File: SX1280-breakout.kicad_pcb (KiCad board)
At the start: 2 copper layers, 16 x 16 mm, 32 parts, among them J1 Conn_01x01, J10 Conn_01x01, J11 Conn_01x01, J12 Conn_01x01, J13 Conn_01x01, J14 Conn_01x01, J15 Conn_01x01, J16 Conn_01x01, J2 Conn_01x01, J3 Conn_01x01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

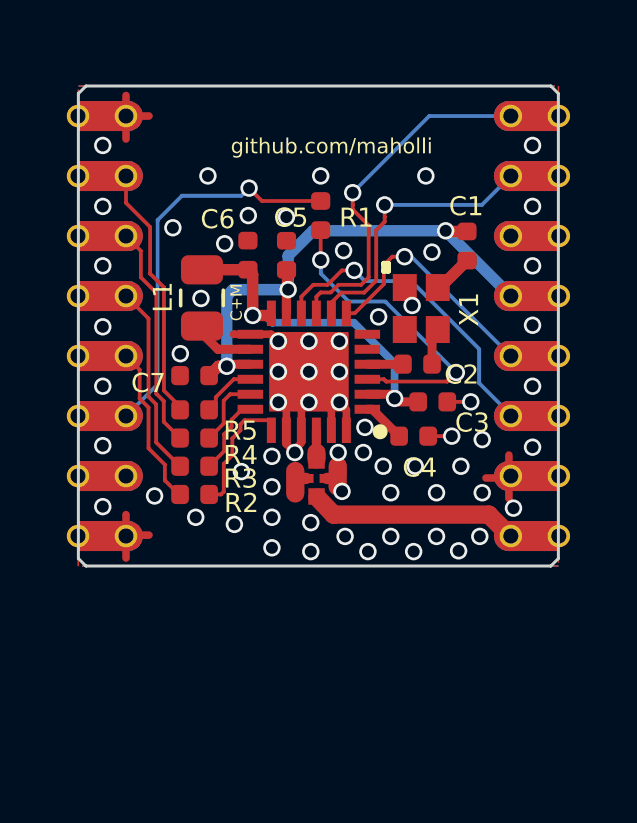
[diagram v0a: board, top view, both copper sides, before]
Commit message: fixing TCXO cap
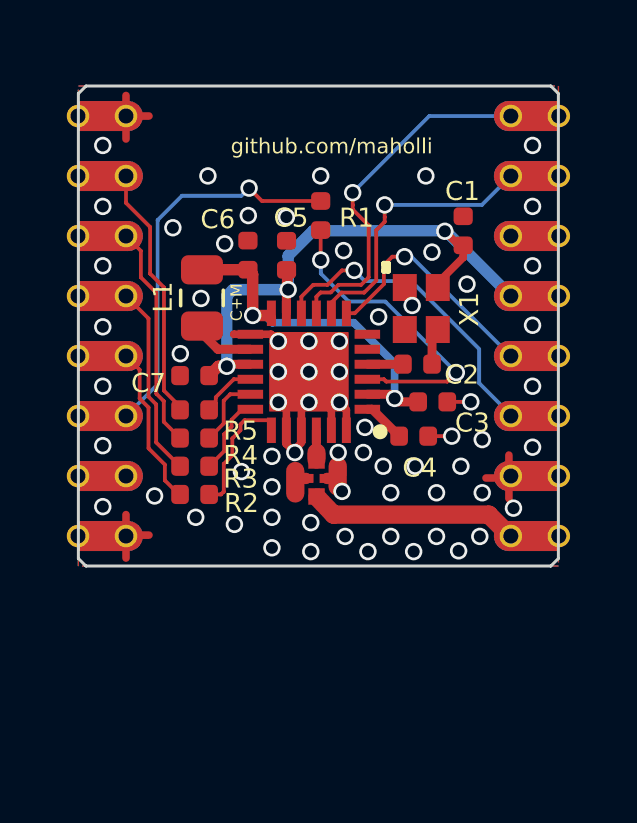
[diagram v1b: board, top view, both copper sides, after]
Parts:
- moved C1 0.52 mm to (111.9, 109.0)
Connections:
- C1 pad 1: +3V3 -> GND
- C1 pad 2: Net-(C1-Pad2) -> +3V3
- X1 pad 4: Net-(C1-Pad2) -> +3V3
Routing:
- net +3V3: track 18.9 -> 20.7 mm
- net Net-(C1-Pad2): track 1.30 -> 0.00 mm
- net GND: vias 67 -> 68

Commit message: updating to v2
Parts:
- moved R5 9.08 mm to (102.4, 105.9), turned to 45 degrees
- moved R4 8.02 mm to (102.4, 107.9), turned to 45 degrees
- moved R3 6.96 mm to (102.4, 109.9), turned to 45 degrees
- moved R1 6.76 mm to (102.7, 113.5), turned to 45 degrees
- moved L1 5.93 mm to (103.5, 117.1), turned to 135 degrees
- moved R2 5.90 mm to (102.4, 111.9), turned to 45 degrees
- moved C7 5.38 mm to (104.7, 118.9), turned to 225 degrees
- moved C6 5.38 mm to (103.6, 115.0), turned to 135 degrees
- moved C1 4.66 mm to (107.4, 110.4), turned to 45 degrees
- moved C5 4.11 mm to (105.1, 113.8), turned to 45 degrees
- moved U2 3.78 mm to (110.5, 118.7), turned to 315 degrees
- moved U1 2.88 mm to (107.8, 116.3), turned to 225 degrees
- moved X1 1.68 mm to (108.9, 112.2), turned to 315 degrees
- moved C4 1.37 mm to (111.3, 116.6), turned to 315 degrees
- moved C3 0.77 mm to (111.6, 114.8), turned to 135 degrees
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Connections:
- net SX_DIO0 renamed Net-(J14-Pad1)
- U2 pad 3: Net-(J9-Pad1) -> Net-(AE1-Pad1)
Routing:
- net Net-(R5-Pad2): track 1.91 -> 20.0 mm, vias 0 -> 2
- net Net-(R4-Pad2): track 2.42 -> 17.6 mm, vias 0 -> 2
- net Net-(R3-Pad2): track 2.63 -> 15.1 mm, vias 0 -> 2
- net SX_RST: track 13.0 -> 2.21 mm, vias 1 -> 0
- net Net-(R2-Pad2): track 4.38 -> 13.8 mm, vias 0 -> 2
- net MISO: track 8.54 -> 1.83 mm
- net MOSI: track 7.48 -> 1.83 mm
- net SCK: track 6.42 -> 1.83 mm
- net Net-(J9-Pad1): track 7.13 -> 2.59 mm
- net GND: track 16.2 -> 20.5 mm, vias 68 -> 37
- net +3V3: track 20.7 -> 24.3 mm
- net SX_CS: track 5.38 -> 1.83 mm
- net SX_DIO1: track 9.40 -> 12.3 mm
- net Net-(R1-Pad2): track 10.5 -> 13.3 mm
- net SX_DIO2: track 11.9 -> 14.4 mm
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- added copper zone on In1.Cu, net GND
- removed copper zone on B.Cu, net GND
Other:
- board size 16 x 16 mm -> 16 x 17 mm
- copper layers 2 -> 4
- board text added: "IO1"
- board text added: "IO2"
- board text added: "IO3"
- board text added: "SX1280 2.4 GHz"
- board text added: "v2"
- board text removed: "SX1280 LoRa"

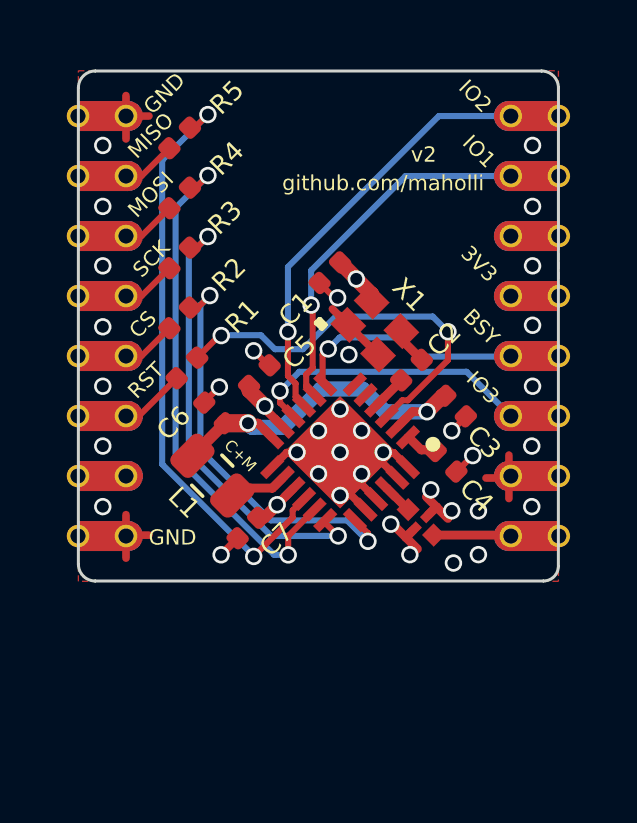
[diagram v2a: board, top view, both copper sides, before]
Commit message: playing with inline RF connector + updating to KiCad6
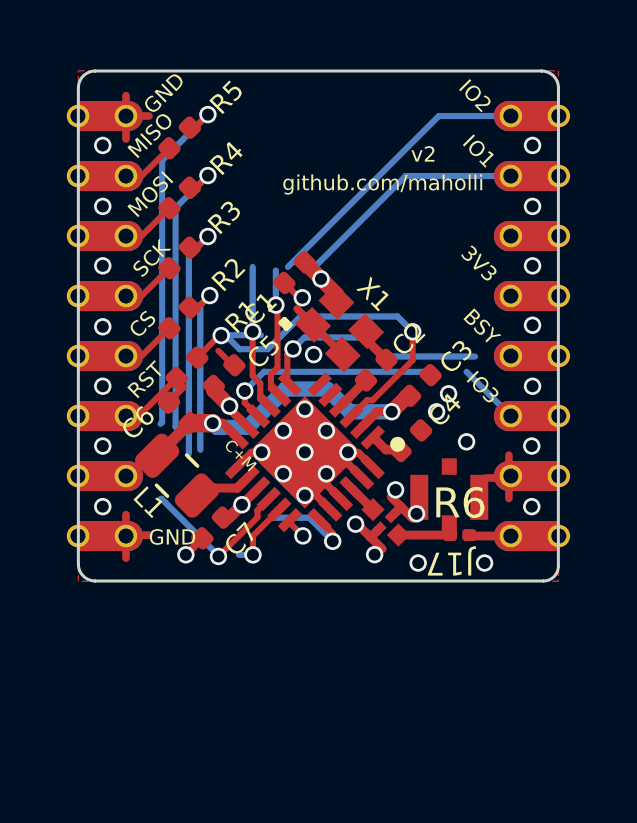
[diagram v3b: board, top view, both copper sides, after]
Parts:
- added J17: Conn_Coaxial, custom-footprints:w.FL, F.Cu at (111.4, 117.9)
- added R6: 0, Resistor_SMD:R_0201_0603Metric, F.Cu at (111.8, 119.1)
- moved C3 1.36 mm to (110.5, 114.1), turned to -135 degrees
- moved C4 1.36 mm to (110.1, 116.0), turned to 45 degrees
- moved C2 1.17 mm to (109.0, 113.6)
- moved C5 1.17 mm to (103.9, 113.8)
- moved C7 1.17 mm to (103.5, 118.9)
- moved L1 1.17 mm to (102.3, 117.1)
- moved U1 1.17 mm to (106.6, 116.3)
- moved U2 1.17 mm to (109.3, 118.7)
- moved X1 1.17 mm to (107.8, 112.2)
- moved C1 1.17 mm to (106.3, 110.4)
- moved C6 1.17 mm to (102.4, 115.0)
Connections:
- C2 pad 2: Net-(C2-Pad2) -> unconnected-(C2-Pad2)
- J14 pad 1: Net-(J14-Pad1) -> unconnected-(J14-Pad1)
- J7 pad 1: Net-(J7-Pad1) -> unconnected-(J7-Pad1)
- U1 pad 5: Net-(U1-Pad5) -> unconnected-(U1-Pad5)
- U1 pad 6: Net-(U1-Pad6) -> unconnected-(U1-Pad6)
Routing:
- net +3V3: track 24.3 -> 10.9 mm
- net Net-(R3-Pad2): track 15.1 -> 8.96 mm
- net Net-(R4-Pad2): track 17.6 -> 11.9 mm
- net SX_DIO2: track 14.4 -> 9.51 mm, vias 1 -> 0
- net Net-(R1-Pad2): track 13.3 -> 18.1 mm, vias 2 -> 3
- net Net-(R2-Pad2): track 13.8 -> 9.37 mm
- net GND: track 20.5 -> 24.1 mm, vias 37 -> 35
- net Net-(R5-Pad2): track 20.0 -> 17.1 mm
- net Net-(J17-Pad1): track 0.00 -> 1.72 mm
- net unconnected-(C2-Pad2): track 0.00 -> 1.35 mm
- net Net-(C2-Pad2): track 1.35 -> 0.00 mm
- net Net-(J9-Pad1): track 2.59 -> 1.40 mm
- net SX_RST: track 2.21 -> 2.94 mm
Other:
- net class Default removed

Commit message: switched to 0.4mm castellations & routed
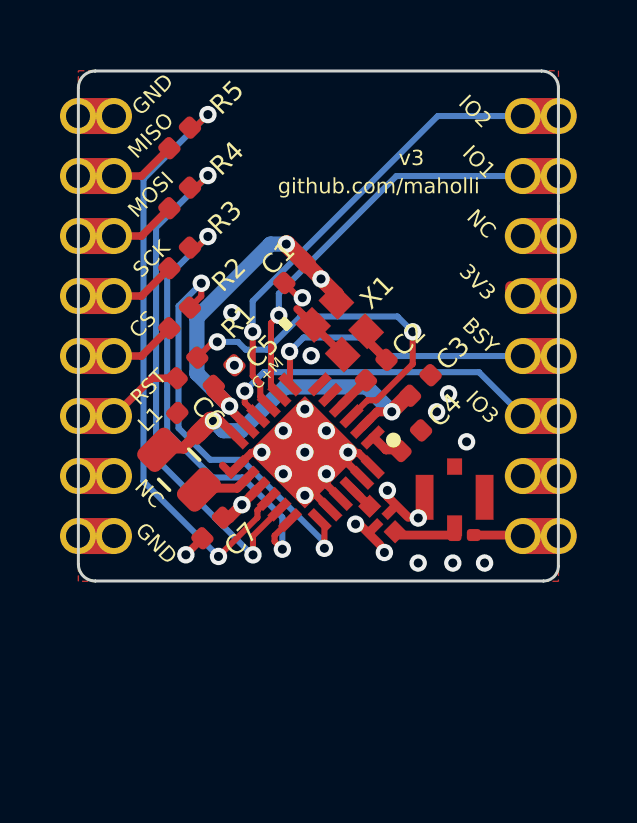
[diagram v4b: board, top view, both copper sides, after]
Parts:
- added Ref**: Val**, custom-footprints:holliday, F.Cu at (106.8, 108.4)
- J1, J10, J11, J12, J13, J14, J15, J16, J2, J3, J4, J5, J6, J7, J8, J9: footprint custom-footprints:castellated -> custom-footprints:castellated_04mm
- moved J14 1.60 mm to (115.1, 109.1)
- moved J10 1.60 mm to (115.1, 117.1)
- moved J11 1.60 mm to (115.1, 115.1)
- moved J12 1.60 mm to (115.1, 113.1)
- moved J13 1.60 mm to (115.1, 111.1)
- moved J15 1.60 mm to (115.1, 107.1)
- moved J16 1.60 mm to (115.1, 105.1)
- moved J9 1.60 mm to (115.1, 119.1)
- moved J1 1.60 mm to (99.0, 105.1)
- moved J2 1.60 mm to (99.0, 107.1)
- moved J3 1.60 mm to (99.0, 109.1)
- moved J4 1.60 mm to (99.0, 111.1)
- moved J5 1.60 mm to (99.0, 113.1)
- moved J6 1.60 mm to (99.0, 115.1)
- moved J7 1.60 mm to (99.0, 117.1)
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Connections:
- C2 pad 2: unconnected-(C2-Pad2) -> Net-(X1-Pad3)
- X1 pad 3: Net-(C2-Pad2) -> Net-(X1-Pad3)
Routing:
- net +3V3: track 10.9 -> 24.2 mm, vias 3 -> 4
- net GND: track 24.1 -> 11.0 mm, vias 35 -> 24
- net Net-(R3-Pad2): track 8.96 -> 15.2 mm
- net Net-(R1-Pad2): track 18.1 -> 12.0 mm, vias 3 -> 2
- net SX_DIO2: track 9.51 -> 15.3 mm, vias 0 -> 1
- net Net-(R4-Pad2): track 11.9 -> 17.4 mm
- net Net-(R2-Pad2): track 9.37 -> 13.8 mm
- net Net-(R5-Pad2): track 17.1 -> 20.0 mm
- net SX_DIO3: track 9.60 -> 11.2 mm
- net SX_BUSY: track 7.97 -> 9.43 mm
- net unconnected-(C2-Pad2): track 1.35 -> 0.00 mm
- net Net-(X1-Pad3): track 0.00 -> 1.35 mm
- net SX_DIO1: track 12.3 -> 13.4 mm
- added copper zone on In2.Cu, net GND
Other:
- board text added: "NC"
- board text added: "v3"
- board text removed: "Holliday"
- board text removed: "v2"

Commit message: generated kikit panel
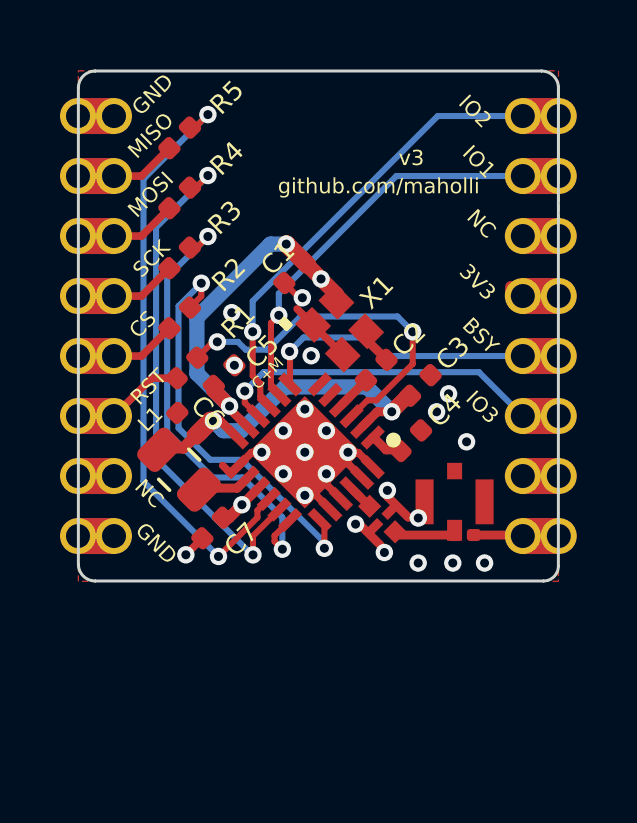
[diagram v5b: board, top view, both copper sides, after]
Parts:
- added REF**: Tab, kikit:Tab, F.Cu at (107.1, 103.4)
- added REF**: Tab, kikit:Tab, F.Cu at (107.1, 120.8)
- moved J17 0.15 mm to (111.6, 118.0)
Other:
- rule pad_to_mask_clearance: 0.0254 -> 0

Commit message: changed to u.FL (undecided)
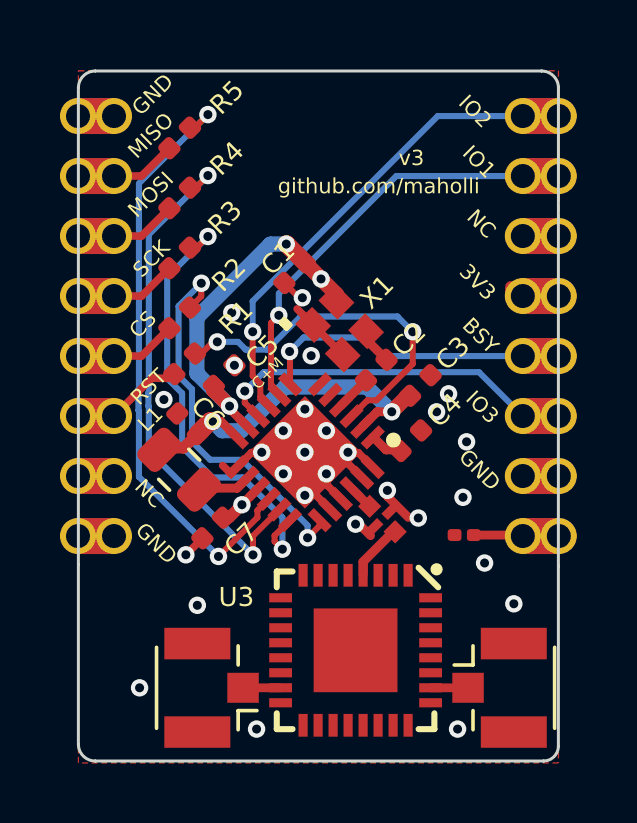
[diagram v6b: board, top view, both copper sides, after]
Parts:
- added J18: u.FL, Connector_Coaxial:U.FL_Hirose_U.FL-R-SMT-1_Vertical, F.Cu at (113.1, 124.2)
- added U3: EP2W+, custom-footprints:QFN32-5X5MM, F.Cu at (108.3, 123.0)
- J17: value Conn_Coaxial -> u.FL; footprint custom-footprints:w.FL -> Connector_Coaxial:U.FL_Hirose_U.FL-R-SMT-1_Vertical
- moved J17 10.2 mm to (103.5, 124.2)
- moved REF** 6.00 mm to (107.1, 126.8)
- moved R1 0.16 mm to (102.6, 113.4)
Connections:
- R6 pad 1: Net-(J17-Pad1) -> unconnected-(R6-Pad1)
- U2 pad 3: Net-(J17-Pad1) -> Net-(U2-Pad3)
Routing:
- net Net-(U2-Pad3): track 0.00 -> 1.93 mm
- net Net-(J18-Pad1): track 0.00 -> 1.25 mm
- net Net-(R2-Pad2): track 13.8 -> 12.9 mm
- net Net-(J17-Pad1): track 1.87 -> 1.25 mm
- net GND: track 11.0 -> 10.7 mm, vias 24 -> 28
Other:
- board size 16 x 17 mm -> 16 x 23 mm
